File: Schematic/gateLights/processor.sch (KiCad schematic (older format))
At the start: 3 parts, among them J2 CONN_02X03, U6 ATTINY1634-SU

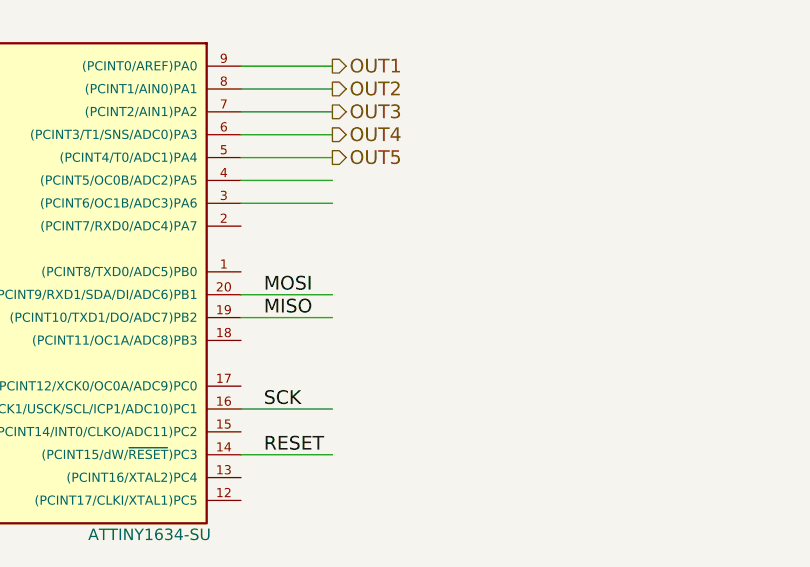
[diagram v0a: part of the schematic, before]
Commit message: RS485 protection
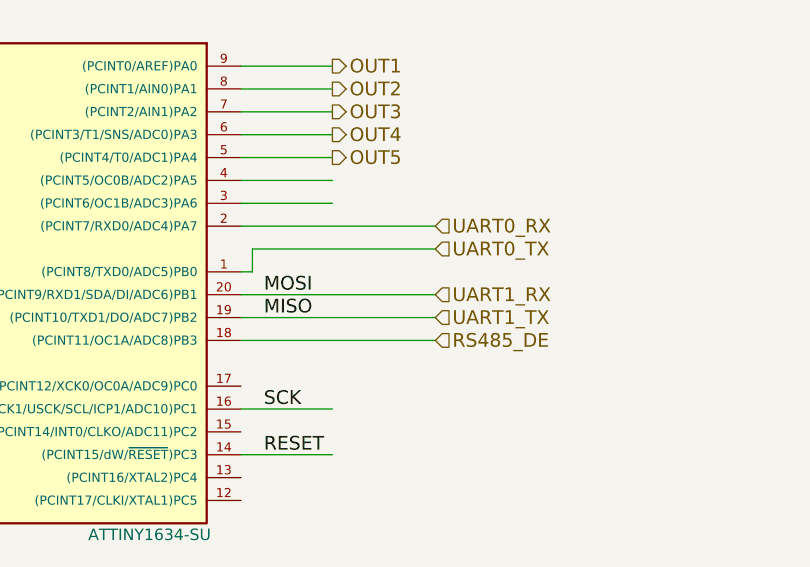
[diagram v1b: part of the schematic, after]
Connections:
- net labels added: RS485_DE, UART0_RX, UART0_TX, UART1_RX, UART1_TX
- wire segments 25 -> 30
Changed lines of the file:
@@
 $EndComp
 $Comp
-L +5V #PWR01
+L +5V #PWR3
 U 1 1 59201E2F
 P 1250 1600
-F 0 "#PWR01" H 1250 1450 50  0001 C CNN
+F 0 "#PWR3" H 1250 1450 50  0001 C CNN
 F 1 "+5V" H 1250 1740 50  0000 C CNN
 F 2 "" H 1250 1600 50  0001 C CNN
@@
 $EndComp
 $Comp
-L GND #PWR02
+L GND #PWR2
 U 1 1 59201EA0
 P 1200 3850
-F 0 "#PWR02" H 1200 3600 50  0001 C CNN
+F 0 "#PWR2" H 1200 3600 50  0001 C CNN
 F 1 "GND" H 1200 3700 50  0000 C CNN
 F 2 "" H 1200 3850 50  0001 C CNN
@@
 RESET
 $Comp
-L +5V #PWR03
+L +5V #PWR6
 U 1 1 5920299B
 P 9700 1500
-F 0 "#PWR03" H 9700 1350 50  0001 C CNN
+F 0 "#PWR6" H 9700 1350 50  0001 C CNN
 F 1 "+5V" H 9700 1640 50  0000 C CNN
 F 2 "" H 9700 1500 50  0001 C CNN
@@
 $EndComp
 $Comp
-L GND #PWR04
+L GND #PWR7
 U 1 1 592029C9
 P 9700 1850
-F 0 "#PWR04" H 9700 1600 50  0001 C CNN
+F 0 "#PWR7" H 9700 1600 50  0001 C CNN
 F 1 "GND" H 9700 1700 50  0000 C CNN
 F 2 "" H 9700 1850 50  0001 C CNN
@@
 	9700 1750 9700 1850
 Wire Wire Line
-	3250 2850 3650 2850
+	3250 2850 4100 2850
 Wire Wire Line
-	3250 2950 3650 2950
+	3250 2950 4100 2950
 Wire Wire Line
 	3250 3350 3650 3350
@@
 $EndComp
 $Comp
-L GND #PWR05
+L GND #PWR5
 U 1 1 592081D8
 P 5950 7100
-F 0 "#PWR05" H 5950 6850 50  0001 C CNN
+F 0 "#PWR5" H 5950 6850 50  0001 C CNN
 F 1 "GND" H 5950 6950 50  0000 C CNN
 F 2 "" H 5950 7100 50  0001 C CNN
@@
 $EndComp
 $Comp
-L +5V #PWR06
+L +5V #PWR4
 U 1 1 592081EC
 P 5950 6450
-F 0 "#PWR06" H 5950 6300 50  0001 C CNN
+F 0 "#PWR4" H 5950 6300 50  0001 C CNN
 F 1 "+5V" H 5950 6590 50  0000 C CNN
 F 2 "" H 5950 6450 50  0001 C CNN
@@
 Wire Wire Line
 	5950 6900 5950 7100
+Text HLabel 4100 2950 2    60   Input ~ 0
+UART1_TX
+Text HLabel 4100 2850 2    60   Input ~ 0
+UART1_RX
+Text HLabel 4100 2550 2    60   Input ~ 0
+UART0_RX
+Text HLabel 4100 2650 2    60   Input ~ 0
+UART0_TX
+Wire Wire Line
+	4100 2550 3250 2550
+Wire Wire Line
+	4100 2650 3300 2650
+Wire Wire Line
+	3300 2650 3300 2750
+Wire Wire Line
+	3300 2750 3250 2750
+Text HLabel 4100 3050 2    60   Input ~ 0
+RS485_DE
+Wire Wire Line
+	4100 3050 3250 3050
 $EndSCHEMATC

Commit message: Add inputs
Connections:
- net labels added: IN_1, IN_2, IN_3
- wire segments 30 -> 32
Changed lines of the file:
@@
 $Descr A4 11693 8268
 encoding utf-8
-Sheet 2 5
+Sheet 2 6
 Title "Processor"
 Date "2017-05-20"
@@
 $EndComp
 $Comp
-L +5V #PWR3
+L +5V #PWR03
 U 1 1 59201E2F
 P 1250 1600
-F 0 "#PWR3" H 1250 1450 50  0001 C CNN
+F 0 "#PWR03" H 1250 1450 50  0001 C CNN
 F 1 "+5V" H 1250 1740 50  0000 C CNN
 F 2 "" H 1250 1600 50  0001 C CNN
@@
 $EndComp
 $Comp
-L GND #PWR2
+L GND #PWR04
 U 1 1 59201EA0
 P 1200 3850
-F 0 "#PWR2" H 1200 3600 50  0001 C CNN
+F 0 "#PWR04" H 1200 3600 50  0001 C CNN
 F 1 "GND" H 1200 3700 50  0000 C CNN
 F 2 "" H 1200 3850 50  0001 C CNN
@@
 RESET
 $Comp
-L +5V #PWR6
+L +5V #PWR05
 U 1 1 5920299B
 P 9700 1500
-F 0 "#PWR6" H 9700 1350 50  0001 C CNN
+F 0 "#PWR05" H 9700 1350 50  0001 C CNN
 F 1 "+5V" H 9700 1640 50  0000 C CNN
 F 2 "" H 9700 1500 50  0001 C CNN
@@
 $EndComp
 $Comp
-L GND #PWR7
+L GND #PWR06
 U 1 1 592029C9
 P 9700 1850
-F 0 "#PWR7" H 9700 1600 50  0001 C CNN
+F 0 "#PWR06" H 9700 1600 50  0001 C CNN
 F 1 "GND" H 9700 1700 50  0000 C CNN
 F 2 "" H 9700 1850 50  0001 C CNN
@@
 	3250 2950 4100 2950
 Wire Wire Line
-	3250 3350 3650 3350
+	3250 3350 4100 3350
 Wire Wire Line
 	3250 3550 3650 3550
@@
 RESET
 Wire Wire Line
-	3250 1850 3650 1850
-Wire Wire Line
-	3250 1950 3650 1950
-Wire Wire Line
-	3250 2050 3650 2050
-Wire Wire Line
-	3250 2150 3650 2150
-Wire Wire Line
-	3250 2250 3650 2250
+	3250 1850 4100 1850
+Wire Wire Line
+	3250 1950 4100 1950
+Wire Wire Line
+	3250 2050 4100 2050
+Wire Wire Line
+	3250 2150 4100 2150
+Wire Wire Line
+	3250 2250 4100 2250
 Wire Wire Line
 	3250 2350 3650 2350
 Wire Wire Line
 	3250 2450 3650 2450
-Text HLabel 3650 1850 2    60   Output ~ 0
+Text HLabel 4100 1850 2    60   Output ~ 0
 OUT1
-Text HLabel 3650 1950 2    60   Output ~ 0
+Text HLabel 4100 1950 2    60   Output ~ 0
 OUT2
-Text HLabel 3650 2050 2    60   Output ~ 0
+Text HLabel 4100 2050 2    60   Output ~ 0
 OUT3
-Text HLabel 3650 2150 2    60   Output ~ 0
+Text HLabel 4100 2150 2    60   Output ~ 0
 OUT4
-Text HLabel 3650 2250 2    60   Output ~ 0
+Text HLabel 4100 2250 2    60   Output ~ 0
 OUT5
 Wire Wire Line
@@
 $EndComp
 $Comp
-L GND #PWR5
+L GND #PWR07
 U 1 1 592081D8
 P 5950 7100
-F 0 "#PWR5" H 5950 6850 50  0001 C CNN
+F 0 "#PWR07" H 5950 6850 50  0001 C CNN
 F 1 "GND" H 5950 6950 50  0000 C CNN
 F 2 "" H 5950 7100 50  0001 C CNN
@@
 $EndComp
 $Comp
-L +5V #PWR4
+L +5V #PWR08
 U 1 1 592081EC
 P 5950 6450
-F 0 "#PWR4" H 5950 6300 50  0001 C CNN
+F 0 "#PWR08" H 5950 6300 50  0001 C CNN
 F 1 "+5V" H 5950 6590 50  0000 C CNN
 F 2 "" H 5950 6450 50  0001 C CNN
@@
 Wire Wire Line
 	4100 3050 3250 3050
+Wire Wire Line
+	3250 3450 4100 3450
+Text HLabel 4100 3250 2    60   Input ~ 0
+IN_1
+Text HLabel 4100 3350 2    60   Input ~ 0
+IN_2
+Text HLabel 4100 3450 2    60   Input ~ 0
+IN_3
+Wire Wire Line
+	3250 3250 4100 3250
 $EndSCHEMATC
